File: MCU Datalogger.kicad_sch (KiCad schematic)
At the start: 25 parts, among them U1 24LC1025, U2 24LC1025, U3 DS1337S_, U4 ATMEGA328P-AU, Y1 Crystal, Y2 Crystal

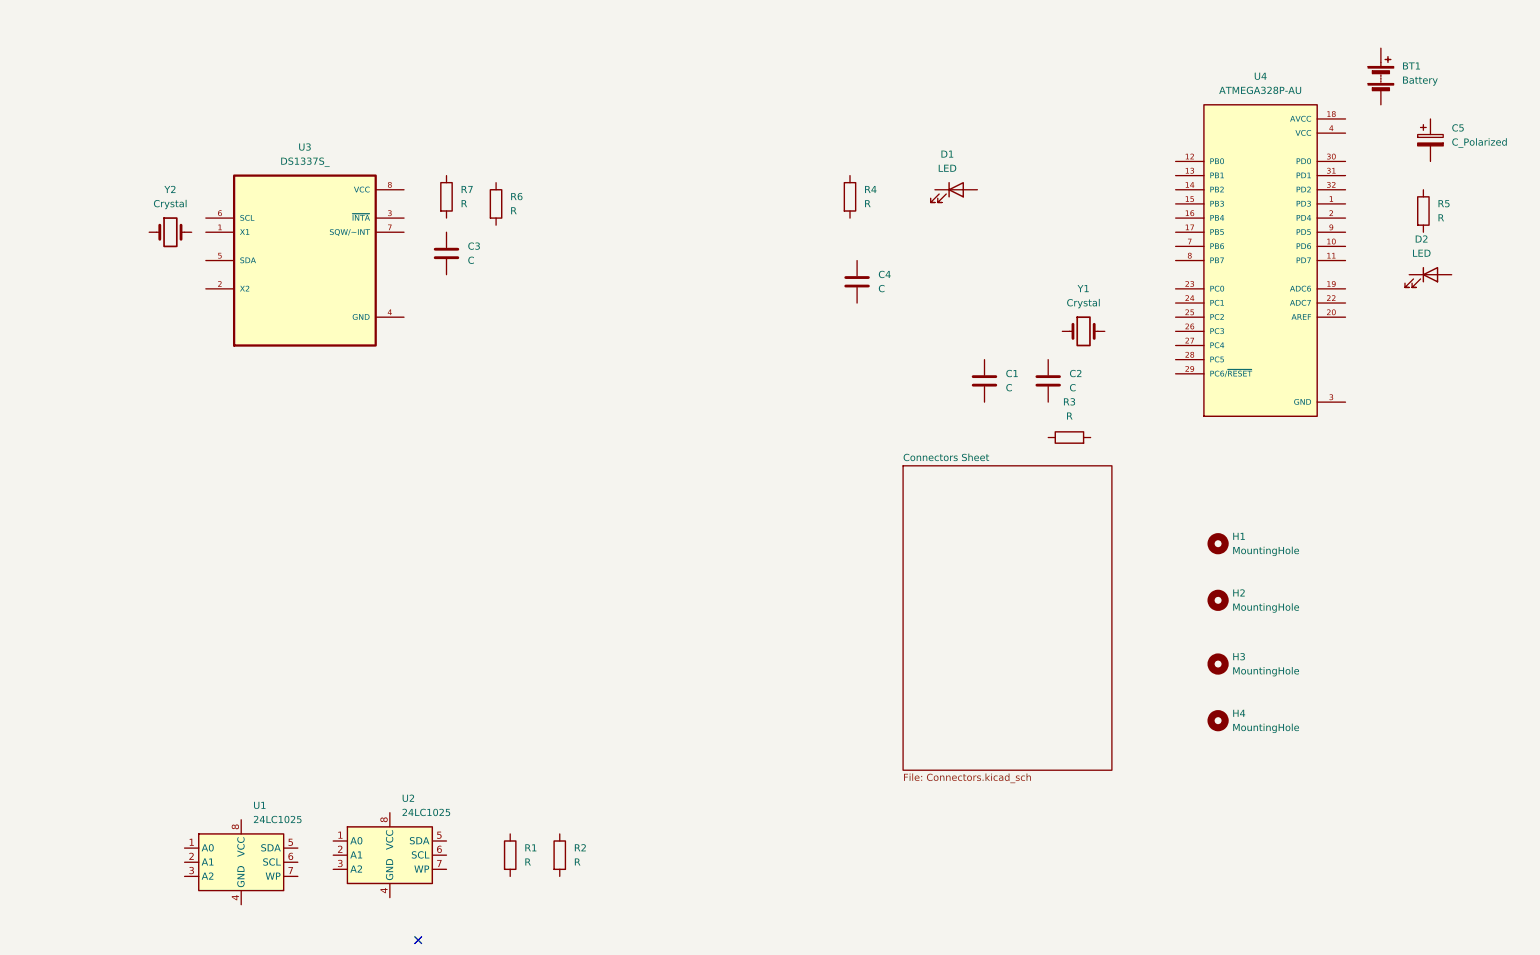
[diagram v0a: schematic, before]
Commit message: Added component Values
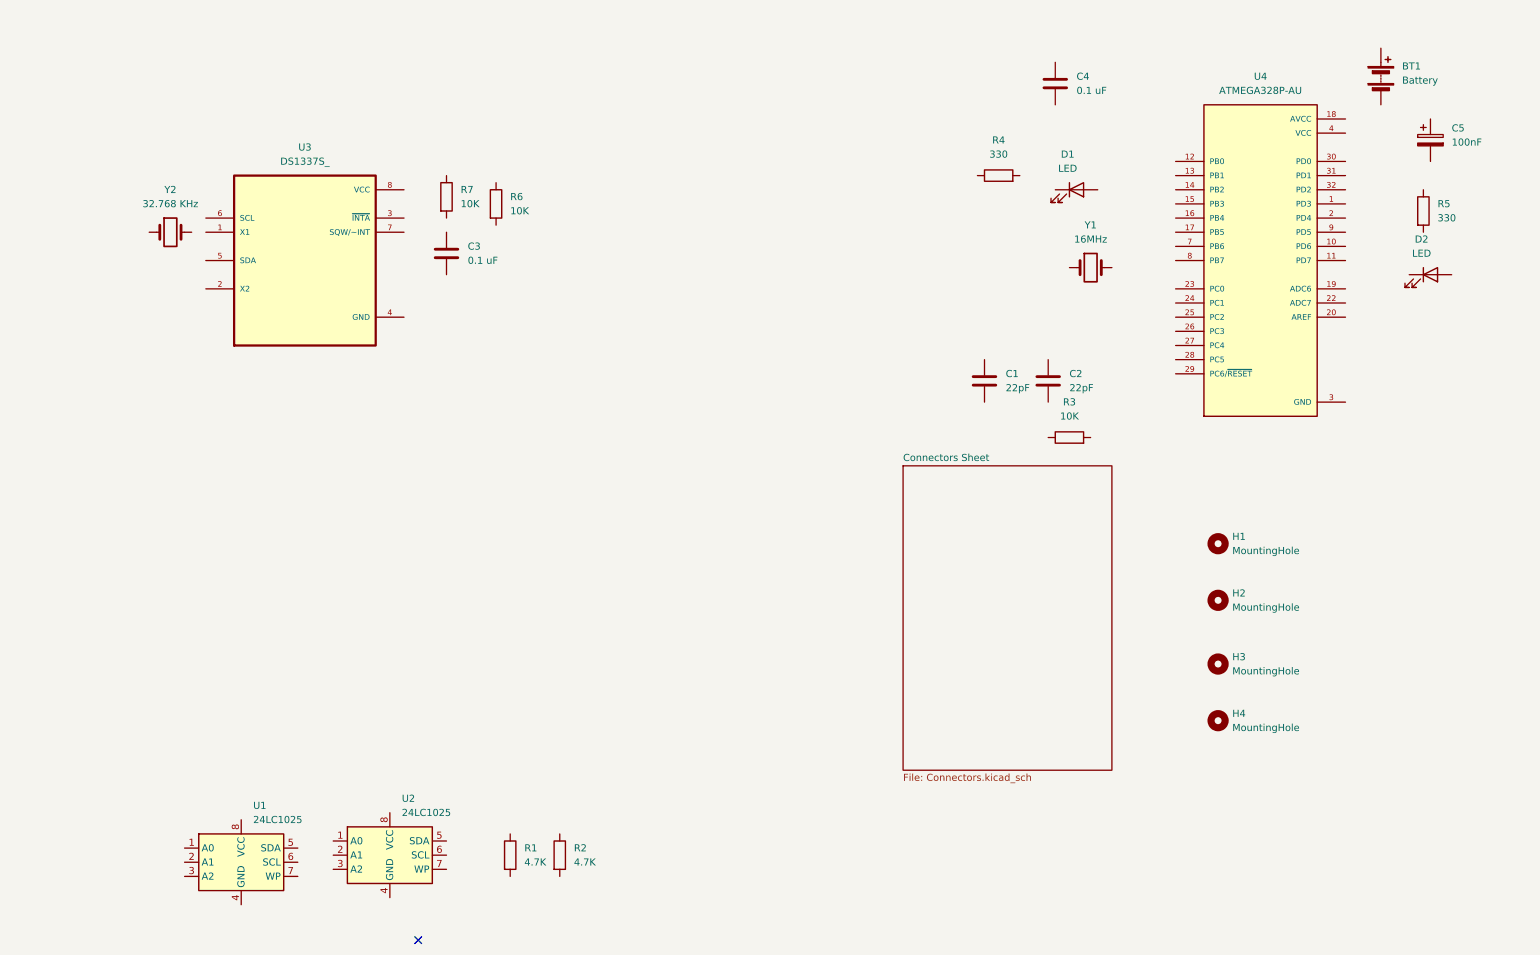
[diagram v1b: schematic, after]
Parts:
- C1, C2: value C -> 22pF
- C3, C4: value C -> 0.1 uF
- C5: value C_Polarized -> 100nF
- R1, R2: value R -> 4.7K
- R3, R6, R7: value R -> 10K
- R4, R5: value R -> 330
- Y1: value Crystal -> 16MHz
- Y2: value Crystal -> 32.768 KHz
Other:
- moved on the sheet: C4, D1, R4, Y1

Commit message: Completed symbol to footprint association
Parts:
- BT1: footprint (none) -> Connector_PinHeader_2.54mm:PinHeader_1x02_P2.54mm_Vertical
- C1, C2, C3, C4, C5: footprint (none) -> Capacitor_SMD:C_0805_2012Metric
- D1, D2: footprint (none) -> LED_SMD:LED_0805_2012Metric
- H1, H2, H3, H4: footprint (none) -> MountingHole:MountingHole_2.1mm
- R1, R2, R3, R4, R5, R6, R7: footprint (none) -> Resistor_SMD:R_0805_2012Metric
- U1, U2: footprint (none) -> Package_SO:SOIC-8_5.3x5.3mm_P1.27mm
- U3: footprint DS1337S_:SOIC127P600X175-8N -> DS1337S:SOIC127P600X175-8N
- Y1, Y2: footprint (none) -> Crystal:Crystal_SMD_5032-2Pin_5.0x3.2mm_HandSoldering
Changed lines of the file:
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@@
 			)
 		)
-		(property "Footprint" ""
+		(property "Footprint" "Capacitor_SMD:C_0805_2012Metric"
 			(at 188.9252 86.36 0)
 			(hide yes)
@@
 			)
 		)
-		(property "Footprint" ""
+		(property "Footprint" "MountingHole:MountingHole_2.1mm"
 			(at 229.87 121.92 0)
 			(hide yes)
@@
 			)
 		)
-		(property "Footprint" ""
+		(property "Footprint" "Crystal:Crystal_SMD_5032-2Pin_5.0x3.2mm_HandSoldering"
 			(at 207.01 62.23 0)
 			(hide yes)
@@
 			)
 		)
-		(property "Footprint" "DS1337S_:SOIC127P600X175-8N"
+		(property "Footprint" "DS1337S:SOIC127P600X175-8N"
 			(at 66.04 60.96 0)
 			(hide yes)
@@
 			)
 		)
-		(property "Footprint" ""
+		(property "Footprint" "LED_SMD:LED_0805_2012Metric"
 			(at 267.97 63.5 0)
 			(hide yes)
@@
 			)
 		)
-		(property "Footprint" ""
+		(property "Footprint" "Resistor_SMD:R_0805_2012Metric"
 			(at 98.552 50.8 90)
 			(hide yes)
@@
 			)
 		)
-		(property "Footprint" ""
+		(property "Footprint" "MountingHole:MountingHole_2.1mm"
 			(at 229.87 111.76 0)
 			(hide yes)
@@
 			)
 		)
-		(property "Footprint" ""
+		(property "Footprint" "Capacitor_SMD:C_0805_2012Metric"
 			(at 201.6252 33.02 0)
 			(hide yes)
@@
 			)
 		)
-		(property "Footprint" ""
+		(property "Footprint" "Resistor_SMD:R_0805_2012Metric"
 			(at 264.922 52.07 90)
 			(hide yes)
@@
 			)
 		)
-		(property "Footprint" ""
+		(property "Footprint" "Resistor_SMD:R_0805_2012Metric"
 			(at 101.092 167.64 90)
 			(hide yes)
@@
 			)
 		)
-		(property "Footprint" ""
+		(property "Footprint" "Package_SO:SOIC-8_5.3x5.3mm_P1.27mm"
 			(at 54.61 168.91 0)
 			(hide yes)
@@
 			)
 		)
-		(property "Footprint" ""
+		(property "Footprint" "MountingHole:MountingHole_2.1mm"
 			(at 229.87 143.51 0)
 			(hide yes)
@@
 			)
 		)
-		(property "Footprint" ""
+		(property "Footprint" "Resistor_SMD:R_0805_2012Metric"
 			(at 109.982 167.64 90)
 			(hide yes)
@@
 			)
 		)
-		(property "Footprint" ""
+		(property "Footprint" "Resistor_SMD:R_0805_2012Metric"
 			(at 89.662 49.53 90)
 			(hide yes)
@@
 			)
 		)
-		(property "Footprint" ""
+		(property "Footprint" "Capacitor_SMD:C_0805_2012Metric"
 			(at 92.4052 63.5 0)
 			(hide yes)
@@
 			)
 		)
-		(property "Footprint" ""
+		(property "Footprint" "Capacitor_SMD:C_0805_2012Metric"
 			(at 200.3552 86.36 0)
 			(hide yes)
@@
 			)
 		)
-		(property "Footprint" ""
+		(property "Footprint" "Capacitor_SMD:C_0805_2012Metric"
 			(at 268.9352 43.18 0)
 			(hide yes)
@@
 			)
 		)
-		(property "Footprint" ""
+		(property "Footprint" "Connector_PinHeader_2.54mm:PinHeader_1x02_P2.54mm_Vertical"
 			(at 259.08 26.416 90)
 			(hide yes)
@@
 			)
 		)
-		(property "Footprint" ""
+		(property "Footprint" "MountingHole:MountingHole_2.1mm"
 			(at 229.87 133.35 0)
 			(hide yes)
@@
 			)
 		)
-		(property "Footprint" ""
+		(property "Footprint" "Crystal:Crystal_SMD_5032-2Pin_5.0x3.2mm_HandSoldering"
 			(at 41.91 55.88 0)
 			(hide yes)
@@
 			)
 		)
-		(property "Footprint" ""
+		(property "Footprint" "Resistor_SMD:R_0805_2012Metric"
 			(at 203.2 94.488 90)
 			(hide yes)
@@
 			)
 		)
-		(property "Footprint" ""
+		(property "Footprint" "Package_SO:SOIC-8_5.3x5.3mm_P1.27mm"
 			(at 81.28 167.64 0)
 			(hide yes)
@@
 			)
 		)
-		(property "Footprint" ""
+		(property "Footprint" "LED_SMD:LED_0805_2012Metric"
 			(at 204.47 48.26 0)
 			(hide yes)
@@
 			)
 		)
-		(property "Footprint" ""
+		(property "Footprint" "Resistor_SMD:R_0805_2012Metric"
 			(at 190.5 47.498 90)
 			(hide yes)

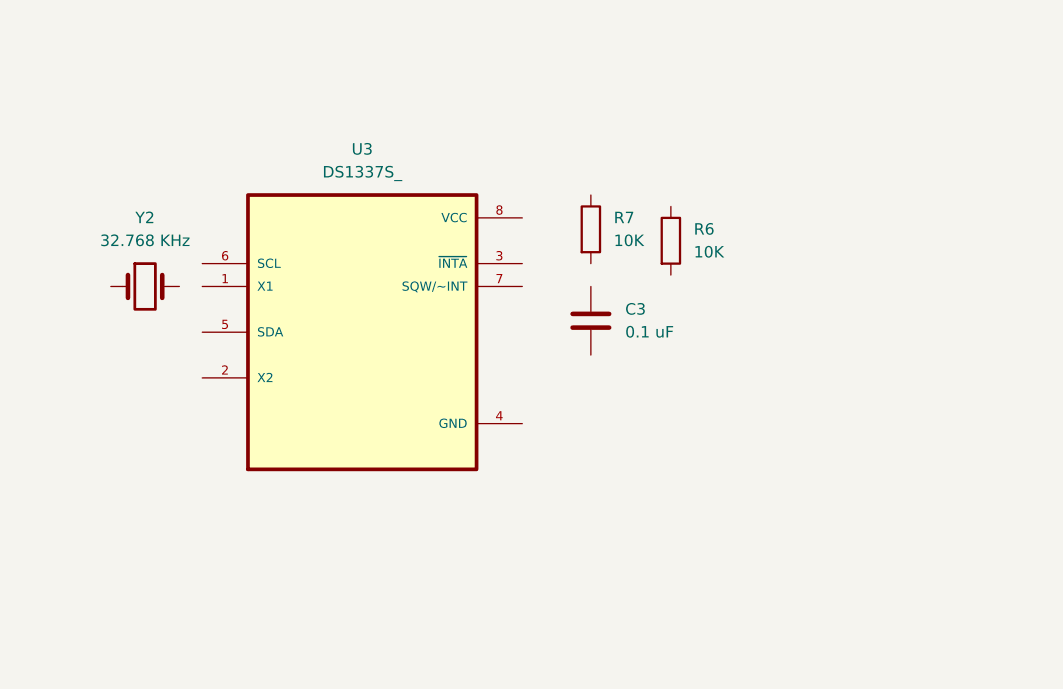
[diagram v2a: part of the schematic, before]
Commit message: Wired the clock
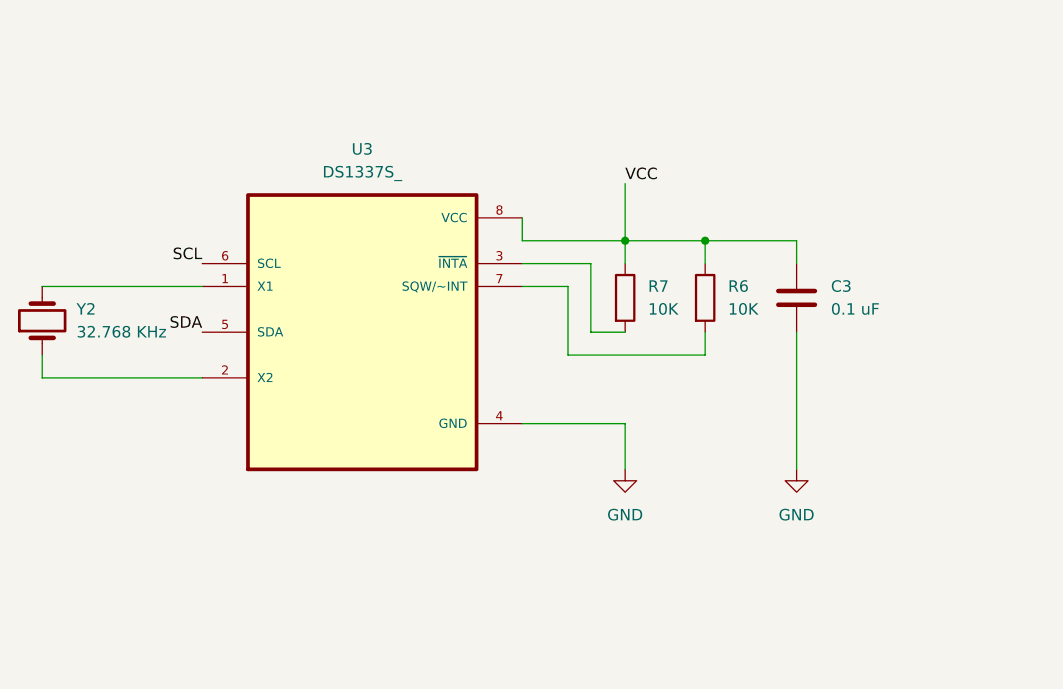
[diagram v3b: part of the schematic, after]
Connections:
- net GND: now also C3.2, U3.4 (GND)
- net VCC: now also C3.1, R6.1, R7.1, U3.8 (VCC)
- net at U3.1 (X1): now also Y2.2
- net at U3.2 (X2): now also Y2.1
- net at U3.3 (~{INTA}): now also R7.2
- net SDA: now reaches U3.5 (SDA)
- net SCL: now reaches U3.6 (SCL)
- net at U3.7 (SQW/~INT): now also R6.2
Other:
- moved on the sheet: C3, R6, R7, Y2

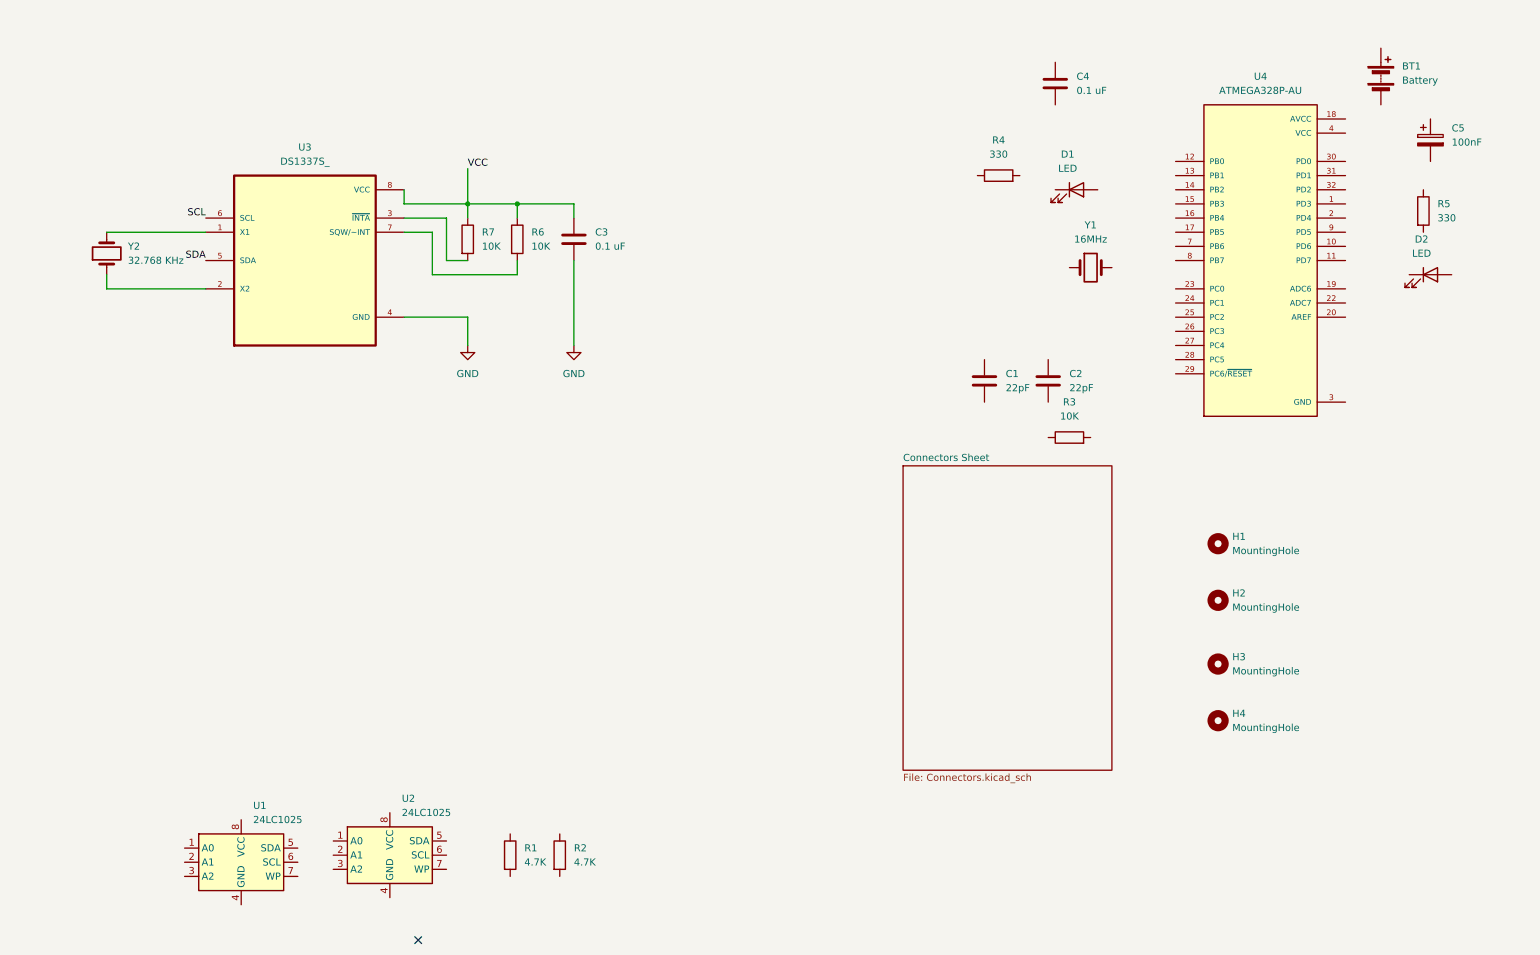
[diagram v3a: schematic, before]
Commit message: Wiring of main sheet
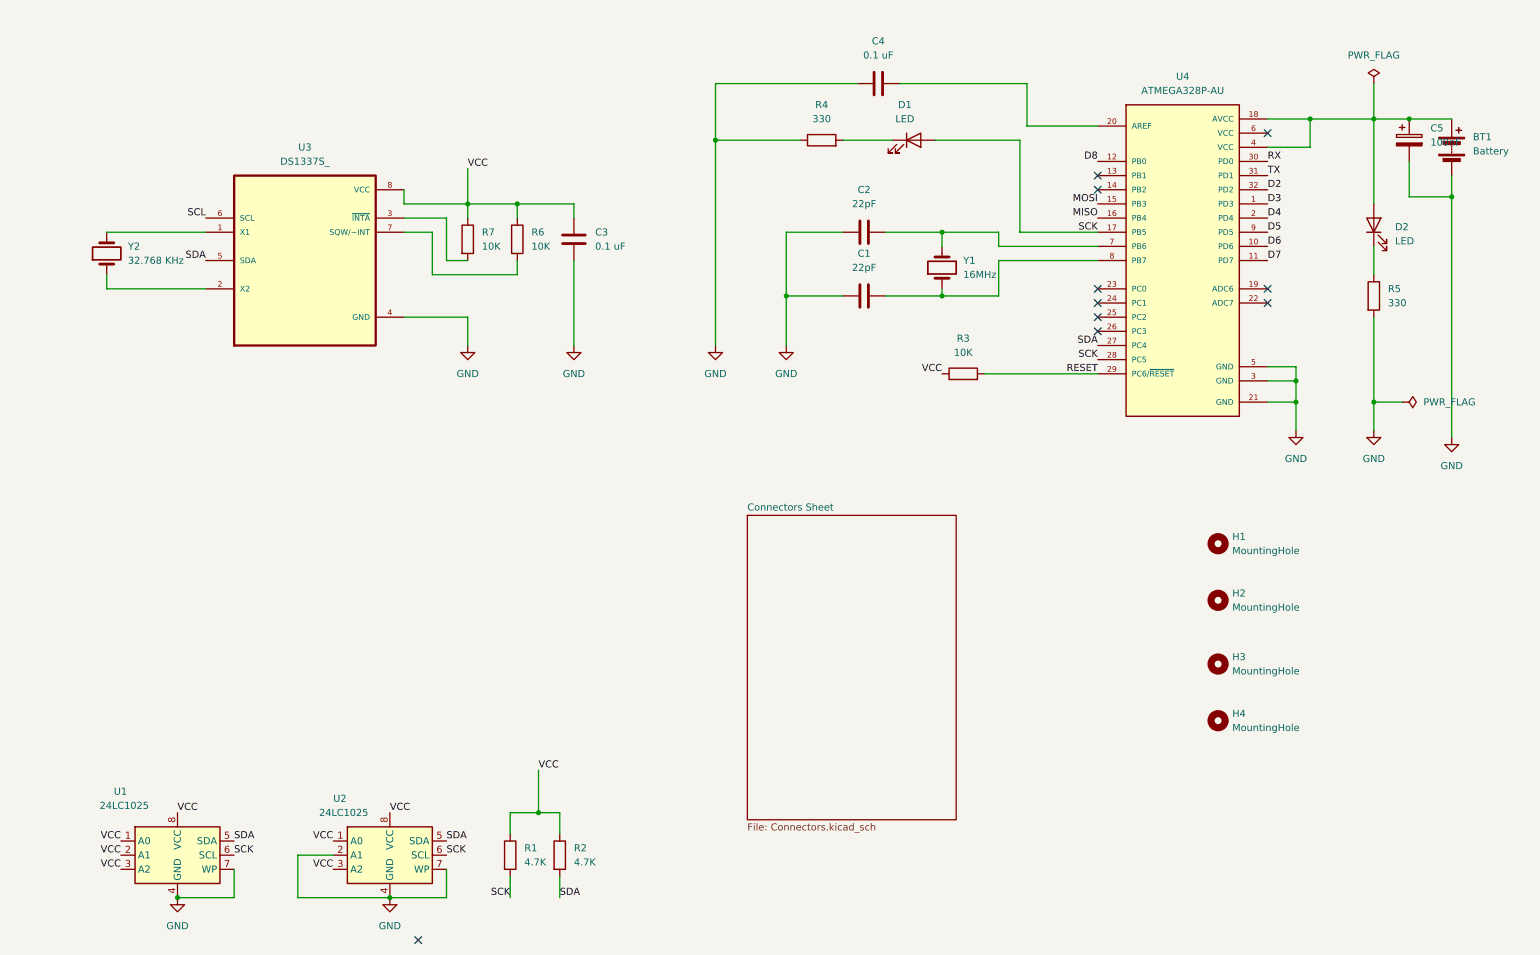
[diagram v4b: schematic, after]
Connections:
- net GND: now also BT1.2 (-), C1.2, C2.1, C4.1, C5.2, R4.1, R5.2, U1.4 (GND), U1.7 (WP), U2.2 (A1), U2.4 (GND), U2.7 (WP)
- net SDA: now also R2.2, U1.5 (SDA), U2.5 (SDA), U4.27 (PC4)
- net VCC: now also R1.1, R2.1, R3.1, U1.1 (A0), U1.2 (A1), U1.3 (A2), U1.8 (VCC), U2.1 (A0), U2.3 (A2), U2.8 (VCC); no longer U4.4 (VCC), U4.6 (VCC)
- net at C1.1: now also U4.8 (PB7), Y1.1
- net at Y1.2: now also C2.2, U4.7 (PB6)
- net D3: now reaches U4.1 (PD3)
- net D6: now reaches U4.10 (PD6)
- net D7: now reaches U4.11 (PD7)
- net D8: now reaches U4.12 (PB0)
- net MOSI: now reaches U4.15 (PB3)
- net MISO: now reaches U4.16 (PB4)
- net SCK: now reaches U4.17 (PB5)
- net SCK: now also D1.2 (A), R1.2, U1.6 (SCL), U2.6 (SCL), U4.28 (PC5)
- net at U4.18 (AVCC): now also BT1.1 (+), C5.1, D2.2 (A), U4.4 (VCC)
- net D4: now reaches U4.2 (PD4)
- net at U4.20 (AREF): now also C4.2
- net RESET: now reaches U4.29 (PC6/~{RESET})
- net RESET: now also R3.2
- net RX: now reaches U4.30 (PD0)
- net TX: now reaches U4.31 (PD1)
- net D2: now reaches U4.32 (PD2)
- net D5: now reaches U4.9 (PD5)
- net at D2.1 (K): now also R5.1
- net at D1.1 (K): now also R4.2
- no-connect marks 1 -> 10
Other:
- moved on the sheet: BT1, C1, C2, C4, C5, D1, D2, R3, R4, R5, U1, Y1
